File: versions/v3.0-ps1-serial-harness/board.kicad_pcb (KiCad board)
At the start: 4 copper layers, 56.3 x 62 mm, 71 parts, among them J1 PS1 DONOR HARNESS / NOT USB, J2 PS1 SERIAL / NOT USB / 3-SIGN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, J3 USB-C USB2 HRO TYPE-C-31-M-12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, Q1 2N7002 DATA OD, Q2 2N7002 ACK OD, Q3 MMBT3904 AUTO-BOOT, Q4 MMBT3904 AUTO-RESET, SW1 RESET K2-1107ST-A4SW-06, SW2 BOOT K2-1107ST-A4SW-06, U1 ESP32-WROOM-32, U2 AP63203WU-7 3.3V 2A PS1 BUCK, U3 AP2112K-3.3 USB LDO, U4 TPS2113APW POWER MUX, U5 CH340C USB-UART, U6 USBLC6-2SC6 ESD

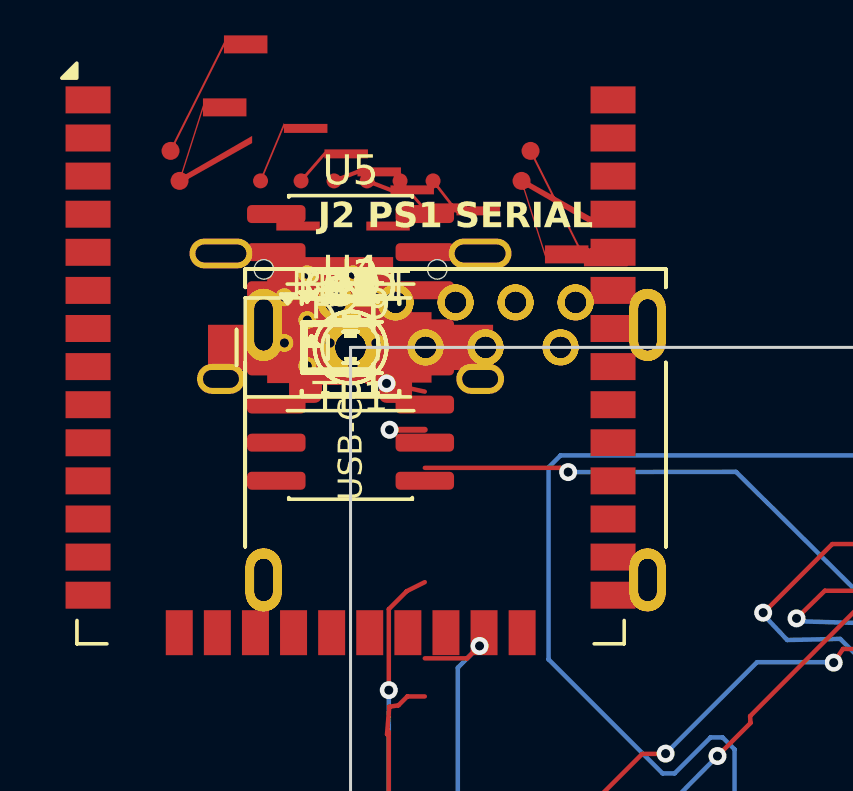
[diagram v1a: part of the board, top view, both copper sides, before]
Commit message: Replace USB-A connectors with stocked C7501856
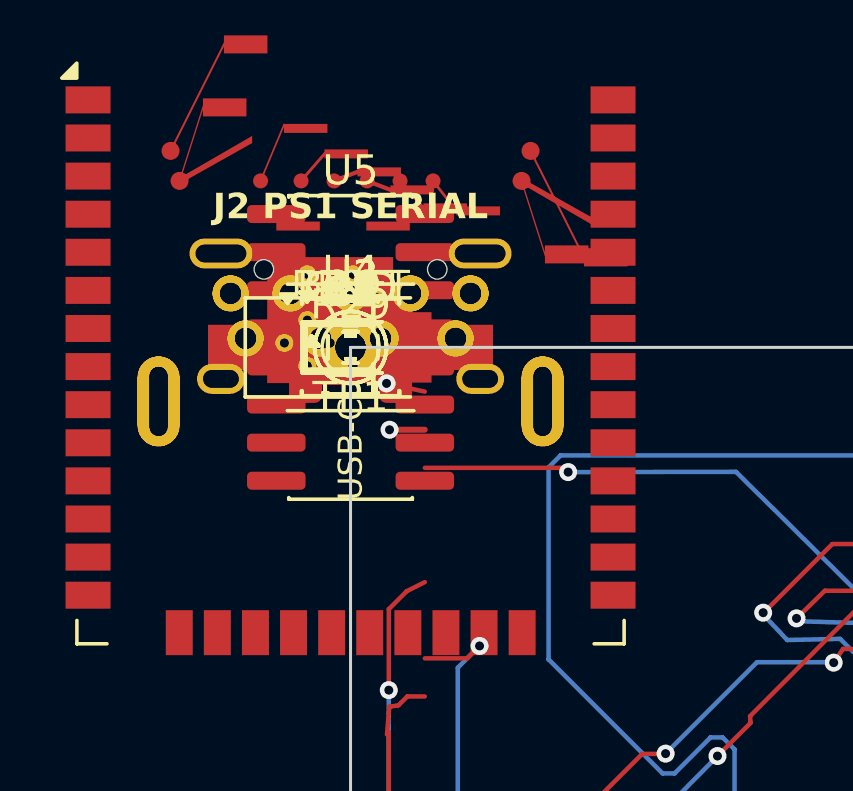
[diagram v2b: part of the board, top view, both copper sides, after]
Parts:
- J1: footprint PlayBridge:USB3_A_Molex_48393-0003_AUTHORIZED_COPY_MODEL_V3 -> PlayBridge:USB3_A_HongCheng_HC-USB3.0-L168-ZP_C7501856_PS1_FRONT_MODEL_V3
- J2: footprint PlayBridge:USB3_A_Molex_48393-0003_PS1_SERIAL_NOT_USB_MODEL_V3 -> PlayBridge:USB3_A_HongCheng_HC-USB3.0-L168-ZP_C7501856_PS1_SERIAL_MODEL_V3

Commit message: Use stocked JLCPCB assembly parts
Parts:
- D1: value STATUS GREEN -> STATUS YELLOW-GREEN
- L1: value 4.7uH >=2.5A SHIELDED -> 4.7uH 2.85A SHIELDED WPN4020H; footprint PlayBridge:L_Sunlord_SWPA4030S -> PlayBridge:L_Sunlord_WPN4020H
- R20: value 700 MUX ILIM -> 680R MUX ILIM
